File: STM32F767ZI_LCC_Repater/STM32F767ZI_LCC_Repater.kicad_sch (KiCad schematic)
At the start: 2 parts, among them CN10 ST_MORPHO, CN7 ST_MORPHO

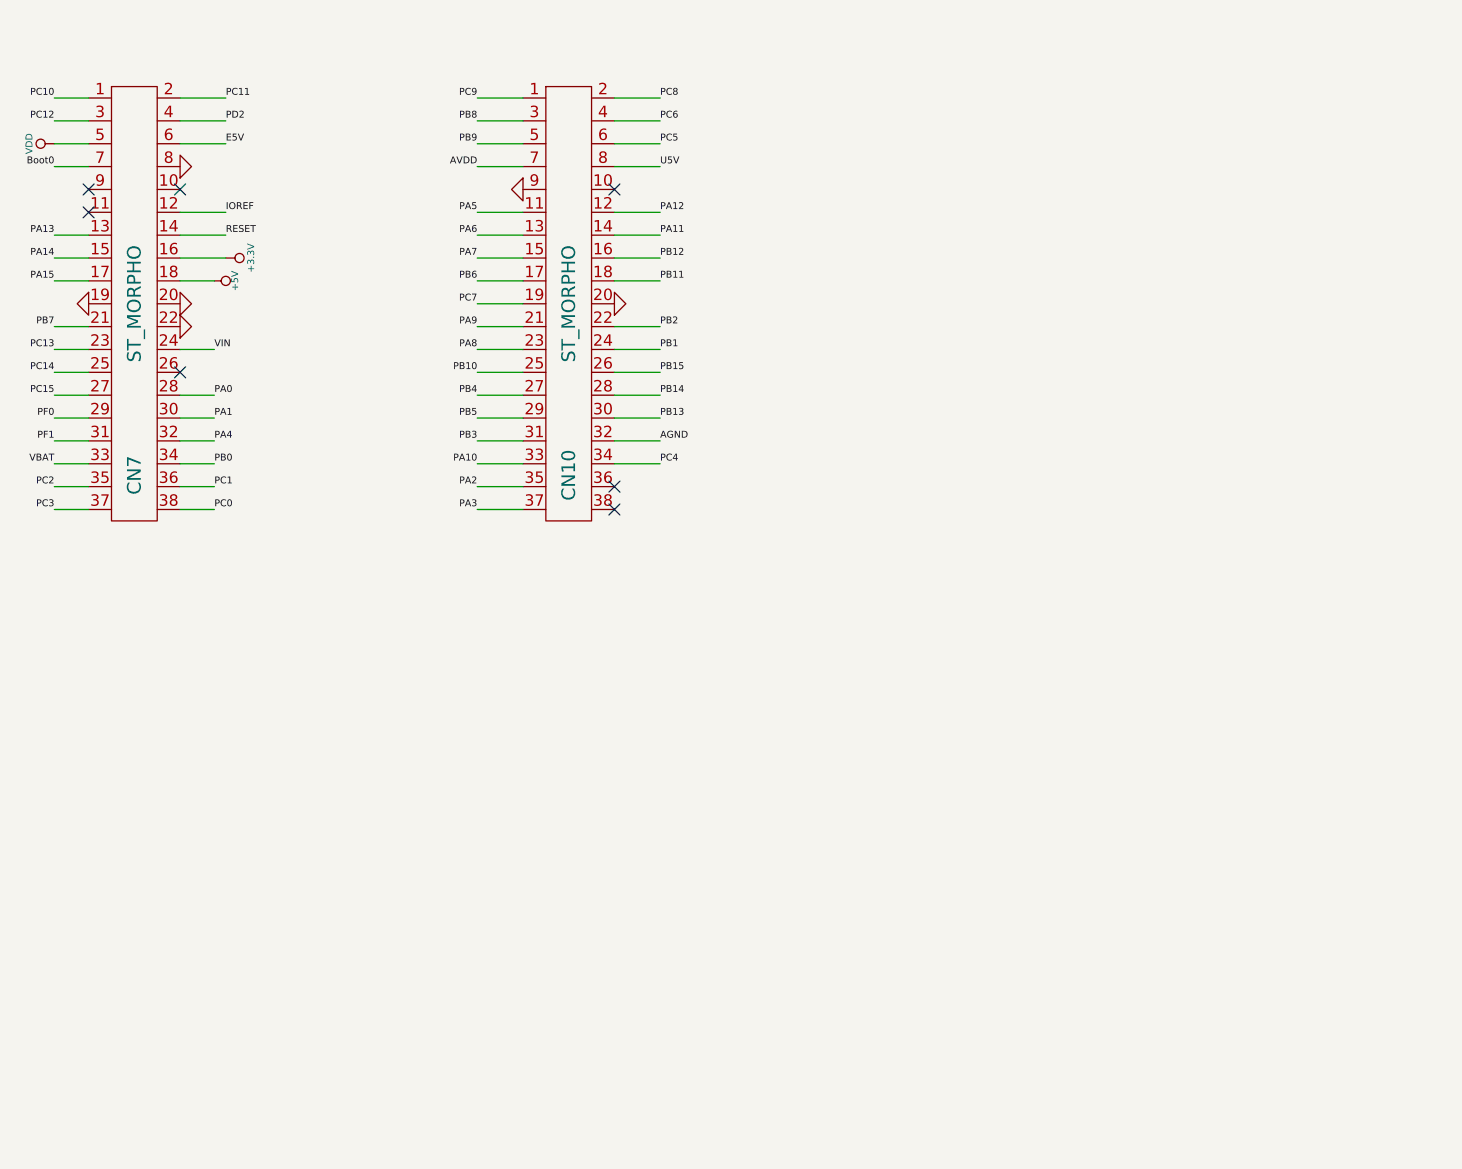
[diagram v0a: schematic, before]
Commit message: Complete STM32F767ZI_LCC_Repater board.
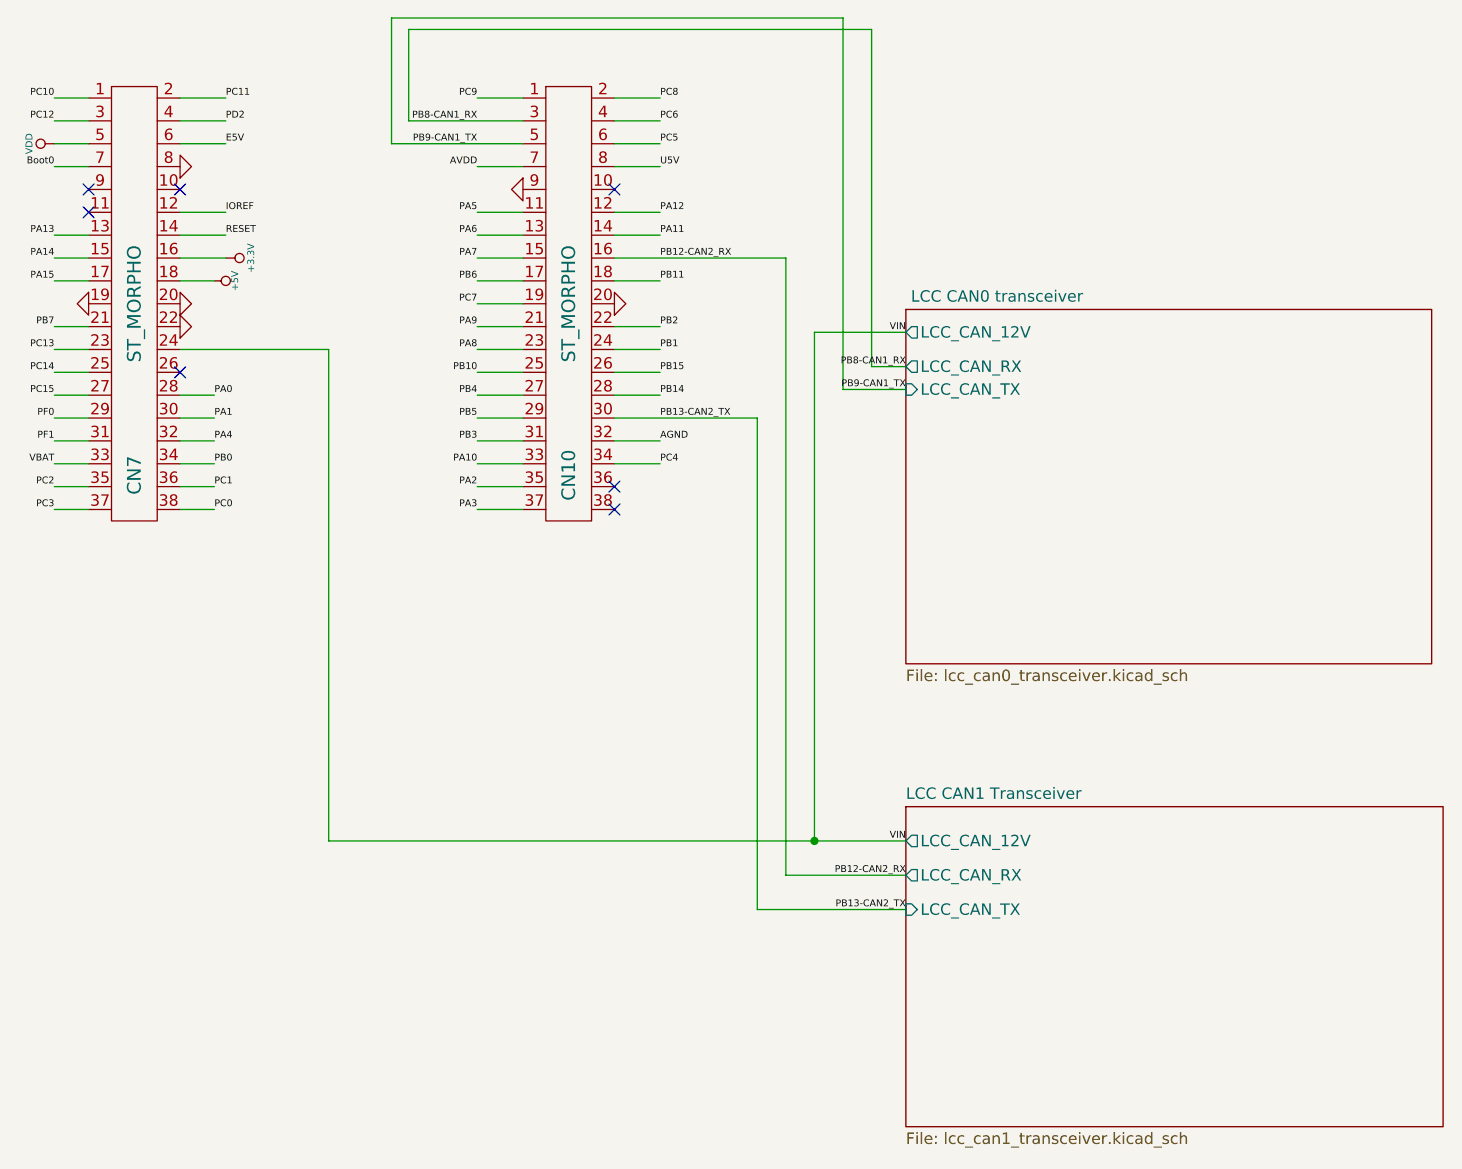
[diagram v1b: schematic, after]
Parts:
- CN10, CN7: footprint (none) -> STMorpho:ST_Morpho
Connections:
- net PB12 renamed PB12-CAN2_RX
- net PB13 renamed PB13-CAN2_TX
- net PB8 renamed PB8-CAN1_RX
- net PB9 renamed PB9-CAN1_TX
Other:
- added sheet  LCC CAN0 transceiver (lcc_can0_transceiver.kicad_sch)
- added sheet LCC CAN1 Transceiver (lcc_can1_transceiver.kicad_sch)
